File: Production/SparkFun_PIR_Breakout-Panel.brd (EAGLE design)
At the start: 204.5 x 152.1 mm, 1853 parts, among them U1 EKMC4607112k, U10 EKMC4607112k, U11 EKMC4607112k, U12 EKMC4607112k, U13 EKMC4607112k, U14 EKMC4607112k, U15 EKMC4607112k, U16 EKMC4607112k, U17 EKMC4607112k, U18 EKMC4607112k, U19 EKMC4607112k, U2 EKMC4607112k, U20 EKMC4607112k, U21 EKMC4607112k, U22 EKMC4607112k, U23 EKMC4607112k, U24 EKMC4607112k, U25 EKMC4607112k, U26 EKMC4607112k, U27 EKMC4607112k, U28 EKMC4607112k, U29 EKMC4607112k, U3 EKMC4607112k, U30 EKMC4607112k, U31 EKMC4607112k, U32 EKMC4607112k, U33 EKMC4607112k, U34 EKMC4607112k, U35 EKMC4607112k, U36 EKMC4607112k, U37 EKMC4607112k, U38 EKMC4607112k, U39 EKMC4607112k, U4 EKMC4607112k, U40 EKMC4607112k, U41 EKMC4607112k, U42 EKMC4607112k, U43 EKMC4607112k, U44 EKMC4607112k, U45 EKMC4607112k, U46 EKMC4607112k, U47 EKMC4607112k, U48 EKMC4607112k, U49 EKMC4607112k, U5 EKMC4607112k, U50 EKMC4607112k, U51 EKMC4607112k, U52 EKMC4607112k, U53 EKMC4607112k, U54 EKMC4607112k, U55 EKMC4607112k, U56 EKMC4607112k, U57 EKMC4607112k, U58 EKMC4607112k, U59 EKMC4607112k, U6 EKMC4607112k, U60 EKMC4607112k, U61 EKMC4607112k, U62 EKMC4607112k, U63 EKMC4607112k, U64 EKMC4607112k, U65 EKMC4607112k, U66 EKMC4607112k, U67 EKMC4607112k, U68 EKMC4607112k, U69 EKMC4607112k, U7 EKMC4607112k, U70 EKMC4607112k, U71 EKMC4607112k, U72 EKMC4607112k, U73 EKMC4607112k, U74 EKMC4607112k, U75 EKMC4607112k, U76 EKMC4607112k, U77 EKMC4607112k, U78 EKMC4607112k, U79 EKMC4607112k, U8 EKMC4607112k, U80 EKMC4607112k, U81 EKMC4607112k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

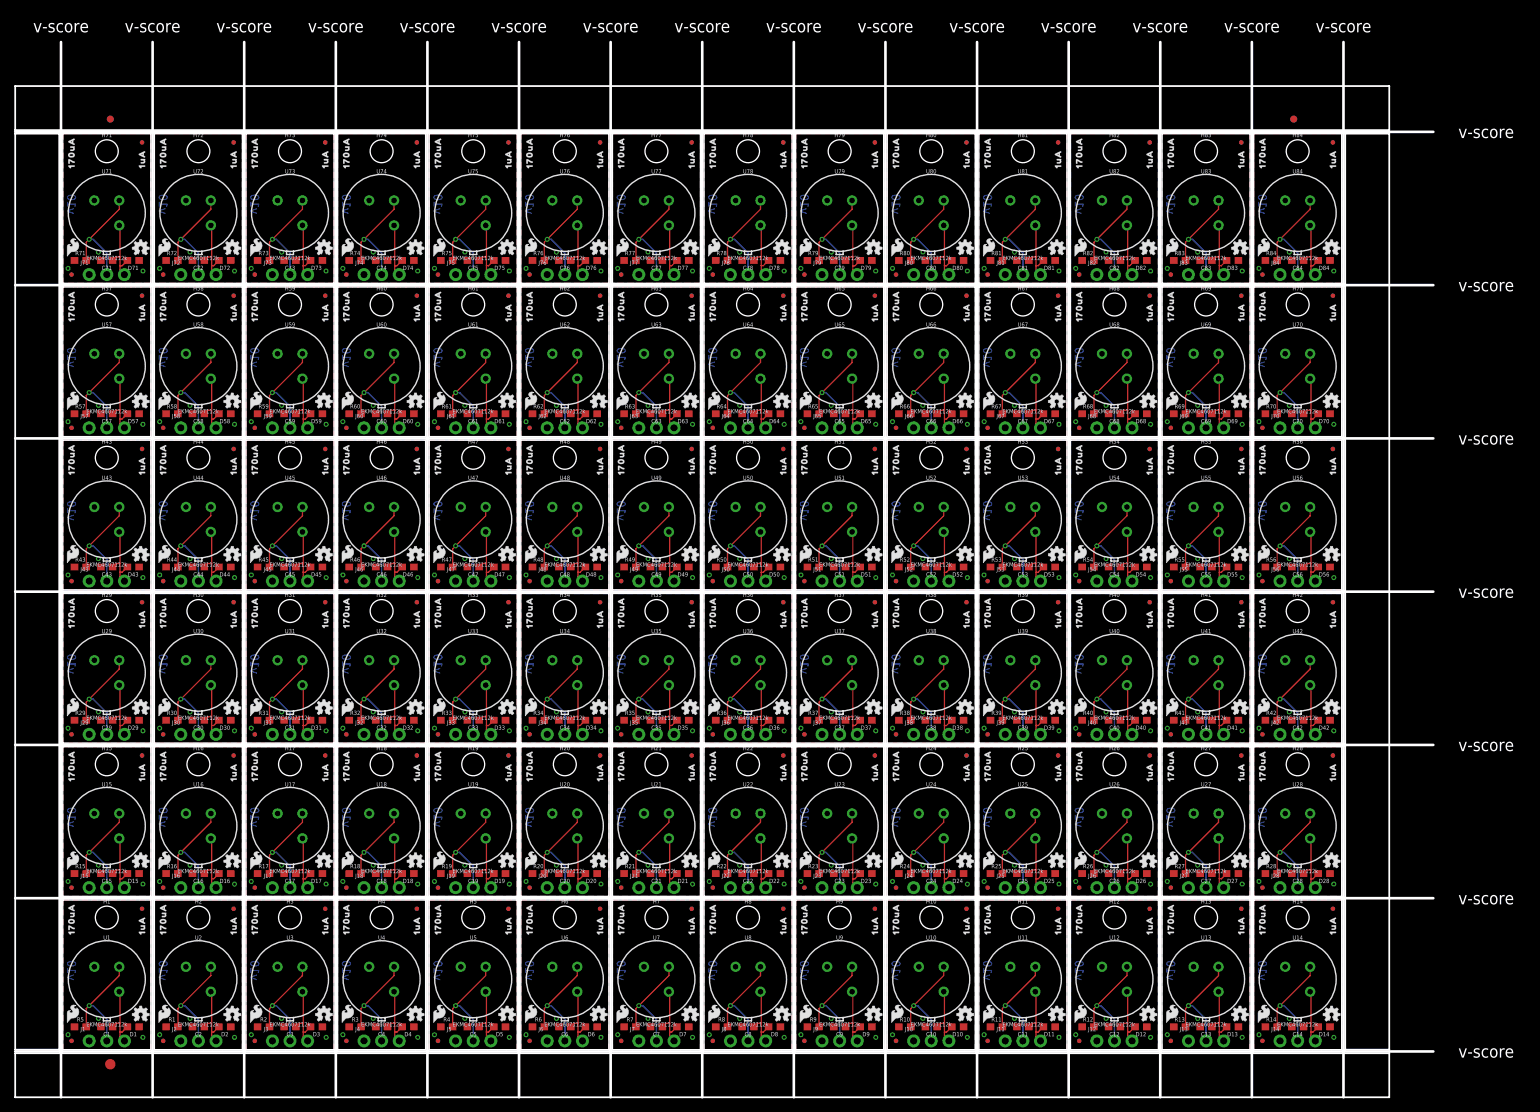
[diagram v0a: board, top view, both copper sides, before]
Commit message: adding fiducial to panel
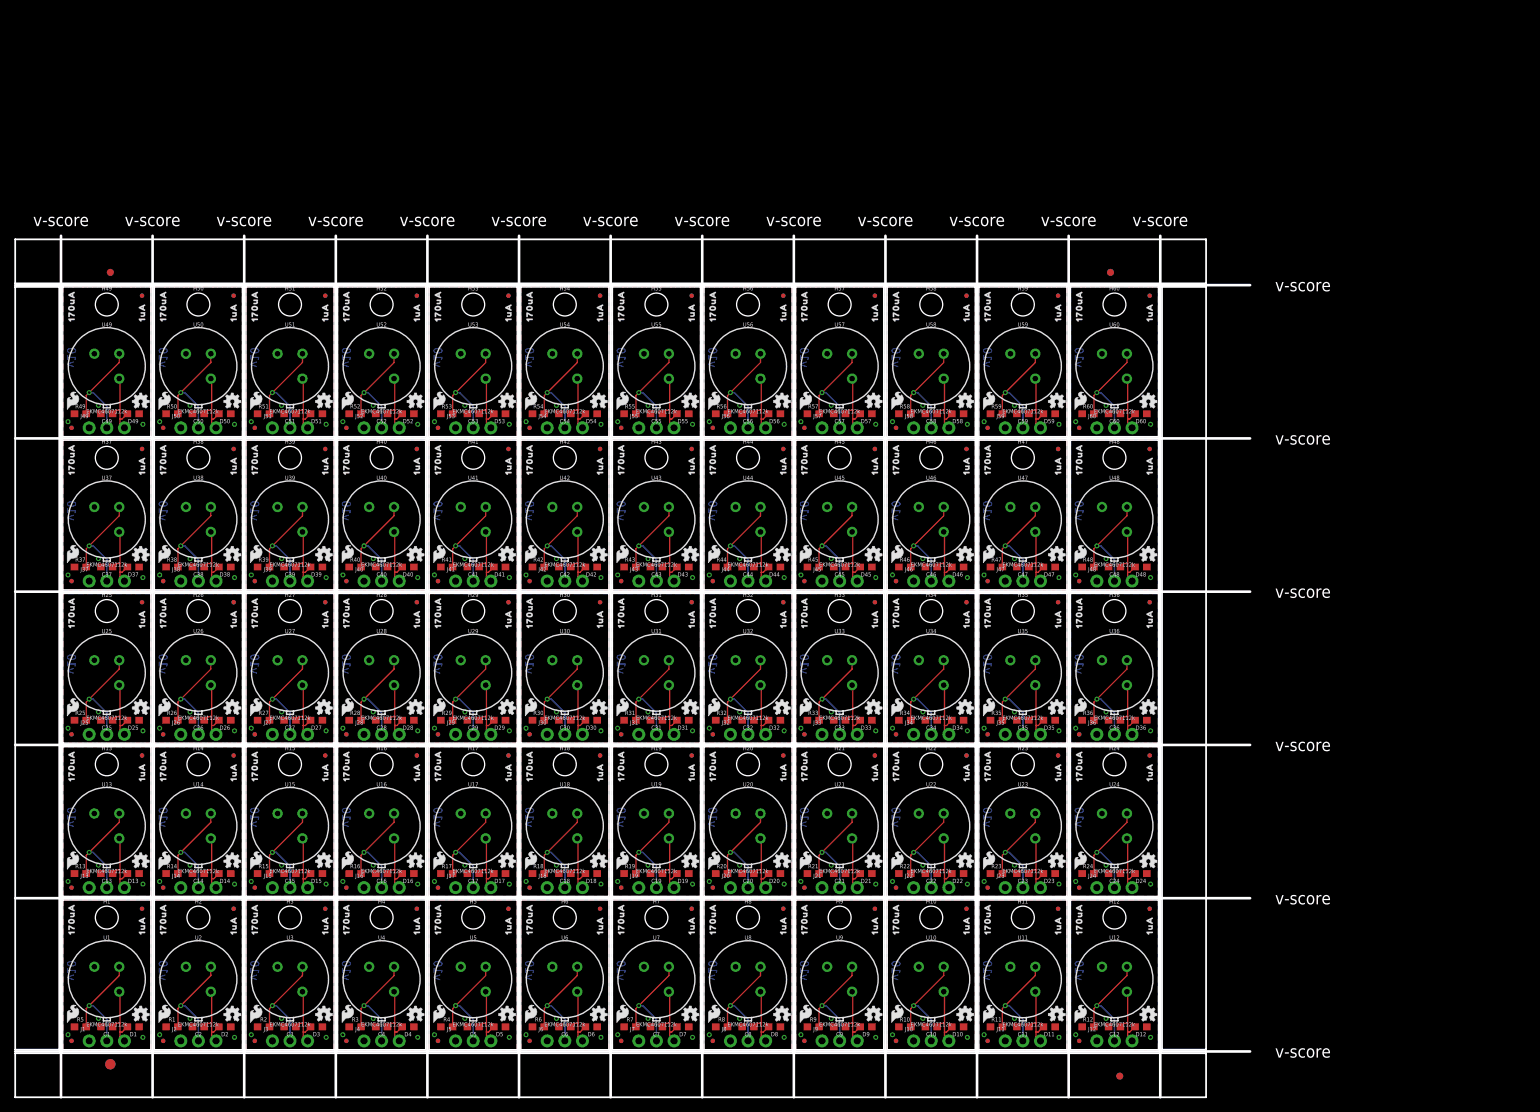
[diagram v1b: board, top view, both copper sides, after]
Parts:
- removed C61, C62, C63, C64, C65, C66, C67, C68, C69, C70, C71, C72, C73, C74, C75, C76, C77, C78, C79, C80, C81, C82, C83, C84: 0.1uF, SparkFun-Capacitors:0603
- removed D61, D62, D63, D64, D65, D66, D67, D68, D69, D70, D71, D72, D73, D74, D75, D76, D77, D78, D79, D80, D81, D82, D83, D84: 24V, SparkFun-DiscreteSemi:0603
- removed H61, H62, H63, H64, H65, H66, H67, H68, H69, H70, H71, H72, H73, H74, H75, H76, H77, H78, H79, H80, H81, H82, H83, H84: STAND-OFF, SparkFun-Hardware:STAND-OFF
- removed J61, J62, J63, J64, J65, J66, J67, J68, J69, J70, J71, J72, J73, J74, J75, J76, J77, J78, J79, J80, J81, J82, J83, J84: (no value), SparkFun-Connectors:1X03_NO_SILK
- removed JP241, JP242, JP243, JP244, JP245, JP246, JP247, JP248, JP249, JP250, JP251, JP252, JP253, JP254, JP255, JP256, JP257, JP258, JP259, JP260, JP261, JP262, JP263, JP264, JP265, JP266, JP267, JP268, JP269, JP270, JP271, JP272, JP273, JP274, JP275, JP276, JP277, JP278, JP279, JP280, JP281, JP282, JP283, JP284, JP285, JP286, JP287, JP288, JP289, JP290, JP291, JP292, JP293, JP294, JP295, JP296, JP297, JP298, JP299, JP300, JP301, JP302, JP303, JP304, JP305, JP306, JP307, JP308, JP309, JP310, JP311, JP312, JP313, JP314, JP315, JP316, JP317, JP318, JP319, JP320, JP321, JP322, JP323, JP324, JP325, JP326, JP327, JP328, JP329, JP330, JP331, JP332, JP333, JP334, JP335, JP336: FIDUCIALUFIDUCIAL, SparkFun:MICRO-FIDUCIAL
- removed LOGO181, LOGO184, LOGO187, LOGO190, LOGO193, LOGO196, LOGO199, LOGO202, LOGO205, LOGO208, LOGO211, LOGO214, LOGO217, LOGO220, LOGO223, LOGO226, LOGO229, LOGO232, LOGO235, LOGO238, LOGO241, LOGO244, LOGO247, LOGO250: OSHW-LOGOMINI, SparkFun-Aesthetics:OSHW-LOGO-MINI
- removed LOGO182, LOGO185, LOGO188, LOGO191, LOGO194, LOGO197, LOGO200, LOGO203, LOGO206, LOGO209, LOGO212, LOGO215, LOGO218, LOGO221, LOGO224, LOGO227, LOGO230, LOGO233, LOGO236, LOGO239, LOGO242, LOGO245, LOGO248, LOGO251: SFE_LOGO_NAME_FLAME.1_INCH, SparkFun-Aesthetics:SFE_LOGO_NAME_FLAME_.1
- removed LOGO183, LOGO186, LOGO189, LOGO192, LOGO195, LOGO198, LOGO201, LOGO204, LOGO207, LOGO210, LOGO213, LOGO216, LOGO219, LOGO222, LOGO225, LOGO228, LOGO231, LOGO234, LOGO237, LOGO240, LOGO243, LOGO246, LOGO249, LOGO252: SFE_LOGO_FLAME.1_INCH, SparkFun-Aesthetics:SFE_LOGO_FLAME_.1
- removed R61, R62, R63, R64, R65, R66, R67, R68, R69, R70, R71, R72, R73, R74, R75, R76, R77, R78, R79, R80, R81, R82, R83, R84: 47k, SparkFun-Resistors:0603
- removed U$541, U$550, U$559, U$568, U$577, U$586, U$595, U$604, U$613, U$622, U$631, U$640, U$649, U$658, U$667, U$676, U$685, U$694, U$703, U$712, U$721, U$730, U$739, U$748: (no value), output:PIR0
- removed U$542, U$551, U$560, U$569, U$578, U$587, U$596, U$605, U$614, U$623, U$632, U$641, U$650, U$659, U$668, U$677, U$686, U$695, U$704, U$713, U$722, U$731, U$740, U$749: (no value), output:170UA0
- removed U$543, U$552, U$561, U$570, U$579, U$588, U$597, U$606, U$615, U$624, U$633, U$642, U$651, U$660, U$669, U$678, U$687, U$696, U$705, U$714, U$723, U$732, U$741, U$750: (no value), output:1UA0
- removed U$544, U$553, U$562, U$571, U$580, U$589, U$598, U$607, U$616, U$625, U$634, U$643, U$652, U$661, U$670, U$679, U$688, U$697, U$706, U$715, U$724, U$733, U$742, U$751: (no value), output:BREAKOUT0
- removed U$545, U$554, U$563, U$572, U$581, U$590, U$599, U$608, U$617, U$626, U$635, U$644, U$653, U$662, U$671, U$680, U$689, U$698, U$707, U$716, U$725, U$734, U$743, U$752: (no value), output:#OUT#0
- removed U$546, U$555, U$564, U$573, U$582, U$591, U$600, U$609, U$618, U$627, U$636, U$645, U$654, U$663, U$672, U$681, U$690, U$699, U$708, U$717, U$726, U$735, U$744, U$753: (no value), output:#3V3#0
- removed U$547, U$556, U$565, U$574, U$583, U$592, U$601, U$610, U$619, U$628, U$637, U$646, U$655, U$664, U$673, U$682, U$691, U$700, U$709, U$718, U$727, U$736, U$745, U$754: (no value), output:#GND#0
- removed U$548, U$557, U$566, U$575, U$584, U$593, U$602, U$611, U$620, U$629, U$638, U$647, U$656, U$665, U$674, U$683, U$692, U$701, U$710, U$719, U$728, U$737, U$746, U$755: (no value), output:X0
- removed U$549, U$558, U$567, U$576, U$585, U$594, U$603, U$612, U$621, U$630, U$639, U$648, U$657, U$666, U$675, U$684, U$693, U$702, U$711, U$720, U$729, U$738, U$747, U$756: (no value), output:Y0
- removed U61, U62, U63, U64, U65, U66, U67, U68, U69, U70, U71, U72, U73, U74, U75, U76, U77, U78, U79, U80, U81, U82, U83, U84: EKMC4607112k, SparkFun-Sensors:TO-3
- added E$6: (no value), SparkFun-Retired:FIDUCIAL-1.5X3
- added E$7, E$8: (no value), SparkFun-Aesthetics:FIDUCIAL-1X2
- moved C13 160.0 mm to (6.35, 25.4)
- moved C14 160.0 mm to (19.6, 25.4)
- moved D13 160.0 mm to (10.2, 25.4)
- moved D14 160.0 mm to (23.4, 25.4)
- moved H13 160.0 mm to (6.35, 41.1)
- moved H14 160.0 mm to (19.6, 41.1)
- moved J13 160.0 mm to (3.81, 23.4)
- moved J14 160.0 mm to (17.0, 23.4)
- moved LOGO37 160.0 mm to (11.2, 27.2)
- moved LOGO38 160.0 mm to (6.35, 36.1)
- moved LOGO39 160.0 mm to (1.46, 27.3)
- moved LOGO40 160.0 mm to (24.4, 27.2)
- moved LOGO41 160.0 mm to (19.6, 36.1)
- moved LOGO42 160.0 mm to (14.7, 27.3)
- moved R13 160.0 mm to (2.54, 25.4)
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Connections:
- removed net 3.3V60: C61.1, D61.2, J61.3, U61.VDD
- removed net 3.3V61: C62.1, D62.2, J62.3, U62.VDD
- removed net 3.3V62: C63.1, D63.2, J63.3, U63.VDD
- removed net 3.3V63: C64.1, D64.2, J64.3, U64.VDD
- removed net 3.3V64: C65.1, D65.2, J65.3, U65.VDD
- removed net 3.3V65: C66.1, D66.2, J66.3, U66.VDD
- removed net 3.3V66: C67.1, D67.2, J67.3, U67.VDD
- removed net 3.3V67: C68.1, D68.2, J68.3, U68.VDD
- removed net 3.3V68: C69.1, D69.2, J69.3, U69.VDD
- removed net 3.3V69: C70.1, D70.2, J70.3, U70.VDD
- removed net 3.3V70: C71.1, D71.2, J71.3, U71.VDD
- removed net 3.3V71: C72.1, D72.2, J72.3, U72.VDD
- removed net 3.3V72: C73.1, D73.2, J73.3, U73.VDD
- removed net 3.3V73: C74.1, D74.2, J74.3, U74.VDD
- removed net 3.3V74: C75.1, D75.2, J75.3, U75.VDD
- removed net 3.3V75: C76.1, D76.2, J76.3, U76.VDD
- removed net 3.3V76: C77.1, D77.2, J77.3, U77.VDD
- removed net 3.3V77: C78.1, D78.2, J78.3, U78.VDD
- removed net 3.3V78: C79.1, D79.2, J79.3, U79.VDD
- removed net 3.3V79: C80.1, D80.2, J80.3, U80.VDD
- removed net 3.3V80: C81.1, D81.2, J81.3, U81.VDD
- removed net 3.3V81: C82.1, D82.2, J82.3, U82.VDD
- removed net 3.3V82: C83.1, D83.2, J83.3, U83.VDD
- removed net 3.3V83: C84.1, D84.2, J84.3, U84.VDD
- removed net GND60: C61.2, D61.1, J61.1, R61.1, U61.GND
- removed net GND61: C62.2, D62.1, J62.1, R62.1, U62.GND
- removed net GND62: C63.2, D63.1, J63.1, R63.1, U63.GND
- removed net GND63: C64.2, D64.1, J64.1, R64.1, U64.GND
- removed net GND64: C65.2, D65.1, J65.1, R65.1, U65.GND
- removed net GND65: C66.2, D66.1, J66.1, R66.1, U66.GND
- removed net GND66: C67.2, D67.1, J67.1, R67.1, U67.GND
- removed net GND67: C68.2, D68.1, J68.1, R68.1, U68.GND
- removed net GND68: C69.2, D69.1, J69.1, R69.1, U69.GND
- removed net GND69: C70.2, D70.1, J70.1, R70.1, U70.GND
- removed net GND70: C71.2, D71.1, J71.1, R71.1, U71.GND
- removed net GND71: C72.2, D72.1, J72.1, R72.1, U72.GND
- removed net GND72: C73.2, D73.1, J73.1, R73.1, U73.GND
- removed net GND73: C74.2, D74.1, J74.1, R74.1, U74.GND
- removed net GND74: C75.2, D75.1, J75.1, R75.1, U75.GND
- removed net GND75: C76.2, D76.1, J76.1, R76.1, U76.GND
- removed net GND76: C77.2, D77.1, J77.1, R77.1, U77.GND
- removed net GND77: C78.2, D78.1, J78.1, R78.1, U78.GND
- removed net GND78: C79.2, D79.1, J79.1, R79.1, U79.GND
- removed net GND79: C80.2, D80.1, J80.1, R80.1, U80.GND
- removed net GND80: C81.2, D81.1, J81.1, R81.1, U81.GND
- removed net GND81: C82.2, D82.1, J82.1, R82.1, U82.GND
- removed net GND82: C83.2, D83.1, J83.1, R83.1, U83.GND
- removed net GND83: C84.2, D84.1, J84.1, R84.1, U84.GND
- removed net PIR_OUT60: J61.2, R61.2, U61.OUT
- removed net PIR_OUT61: J62.2, R62.2, U62.OUT
- removed net PIR_OUT62: J63.2, R63.2, U63.OUT
- removed net PIR_OUT63: J64.2, R64.2, U64.OUT
- removed net PIR_OUT64: J65.2, R65.2, U65.OUT
- removed net PIR_OUT65: J66.2, R66.2, U66.OUT
- removed net PIR_OUT66: J67.2, R67.2, U67.OUT
- removed net PIR_OUT67: J68.2, R68.2, U68.OUT
- removed net PIR_OUT68: J69.2, R69.2, U69.OUT
- removed net PIR_OUT69: J70.2, R70.2, U70.OUT
- removed net PIR_OUT70: J71.2, R71.2, U71.OUT
- removed net PIR_OUT71: J72.2, R72.2, U72.OUT
- removed net PIR_OUT72: J73.2, R73.2, U73.OUT
- removed net PIR_OUT73: J74.2, R74.2, U74.OUT
- removed net PIR_OUT74: J75.2, R75.2, U75.OUT
- removed net PIR_OUT75: J76.2, R76.2, U76.OUT
- removed net PIR_OUT76: J77.2, R77.2, U77.OUT
- removed net PIR_OUT77: J78.2, R78.2, U78.OUT
- removed net PIR_OUT78: J79.2, R79.2, U79.OUT
- removed net PIR_OUT79: J80.2, R80.2, U80.OUT
- removed net PIR_OUT80: J81.2, R81.2, U81.OUT
- removed net PIR_OUT81: J82.2, R82.2, U82.OUT
- removed net PIR_OUT82: J83.2, R83.2, U83.OUT
- removed net PIR_OUT83: J84.2, R84.2, U84.OUT
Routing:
- net PIR_OUT80: track 17.1 -> 0.00 mm, vias 1 -> 0
- net PIR_OUT66: track 17.1 -> 0.00 mm, vias 1 -> 0
- net PIR_OUT75: track 17.1 -> 0.00 mm, vias 1 -> 0
- net PIR_OUT61: track 17.1 -> 0.00 mm, vias 1 -> 0
- net PIR_OUT70: track 17.1 -> 0.00 mm, vias 1 -> 0
- net PIR_OUT74: track 17.1 -> 0.00 mm, vias 1 -> 0
- net PIR_OUT73: track 17.1 -> 0.00 mm, vias 1 -> 0
- net PIR_OUT72: track 17.1 -> 0.00 mm, vias 1 -> 0
- net PIR_OUT71: track 17.1 -> 0.00 mm, vias 1 -> 0
- net PIR_OUT60: track 17.1 -> 0.00 mm, vias 1 -> 0
- net PIR_OUT79: track 17.1 -> 0.00 mm, vias 1 -> 0
- net PIR_OUT78: track 17.1 -> 0.00 mm, vias 1 -> 0
- net PIR_OUT77: track 17.1 -> 0.00 mm, vias 1 -> 0
- net PIR_OUT65: track 17.1 -> 0.00 mm, vias 1 -> 0
- net PIR_OUT64: track 17.1 -> 0.00 mm, vias 1 -> 0
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- removed copper zone on layer 1, net GND60
- removed copper zone on layer 16, net GND60
- removed copper zone on layer 1, net GND61
- removed copper zone on layer 16, net GND61
- removed copper zone on layer 1, net GND62
- removed copper zone on layer 16, net GND62
- removed copper zone on layer 1, net GND63
- removed copper zone on layer 16, net GND63
- removed copper zone on layer 1, net GND64
- removed copper zone on layer 16, net GND64
- removed copper zone on layer 1, net GND65
- removed copper zone on layer 16, net GND65
- removed copper zone on layer 1, net GND66
- removed copper zone on layer 16, net GND66
- removed copper zone on layer 1, net GND67
- removed copper zone on layer 16, net GND67
- removed copper zone on layer 1, net GND68
- removed copper zone on layer 16, net GND68
- removed copper zone on layer 1, net GND69
- removed copper zone on layer 16, net GND69
- removed copper zone on layer 1, net GND70
- removed copper zone on layer 16, net GND70
- removed copper zone on layer 1, net GND71
- removed copper zone on layer 16, net GND71
- removed copper zone on layer 1, net GND72
- removed copper zone on layer 16, net GND72
- removed copper zone on layer 1, net GND73
- removed copper zone on layer 16, net GND73
- removed copper zone on layer 1, net GND74
- removed copper zone on layer 16, net GND74
- removed copper zone on layer 1, net GND75
- removed copper zone on layer 16, net GND75
- removed copper zone on layer 1, net GND76
- removed copper zone on layer 16, net GND76
- removed copper zone on layer 1, net GND77
- removed copper zone on layer 16, net GND77
- removed copper zone on layer 1, net GND78
- removed copper zone on layer 16, net GND78
- removed copper zone on layer 1, net GND79
- removed copper zone on layer 16, net GND79
- removed copper zone on layer 1, net GND80
- removed copper zone on layer 16, net GND80
- removed copper zone on layer 1, net GND81
- removed copper zone on layer 16, net GND81
- removed copper zone on layer 1, net GND82
- removed copper zone on layer 16, net GND82
- removed copper zone on layer 1, net GND83
- removed copper zone on layer 16, net GND83
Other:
- board size 204.5 x 152.1 mm -> 178.1 x 124.2 mm

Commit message: removing fiducial
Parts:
- removed E$7, E$8: (no value), SparkFun-Aesthetics:FIDUCIAL-1X2
- added C61, C62, C63, C64, C65, C66, C67, C68, C69, C70, C71, C72, C73, C74, C75, C76, C77, C78, C79, C80, C81, C82, C83, C84: 0.1uF, SparkFun-Capacitors:0603
- added D61, D62, D63, D64, D65, D66, D67, D68, D69, D70, D71, D72, D73, D74, D75, D76, D77, D78, D79, D80, D81, D82, D83, D84: 24V, SparkFun-DiscreteSemi:0603
- added H61, H62, H63, H64, H65, H66, H67, H68, H69, H70, H71, H72, H73, H74, H75, H76, H77, H78, H79, H80, H81, H82, H83, H84: STAND-OFF, SparkFun-Hardware:STAND-OFF
- added J61, J62, J63, J64, J65, J66, J67, J68, J69, J70, J71, J72, J73, J74, J75, J76, J77, J78, J79, J80, J81, J82, J83, J84: (no value), SparkFun-Connectors:1X03_NO_SILK
- added JP241, JP242, JP243, JP244, JP245, JP246, JP247, JP248, JP249, JP250, JP251, JP252, JP253, JP254, JP255, JP256, JP257, JP258, JP259, JP260, JP261, JP262, JP263, JP264, JP265, JP266, JP267, JP268, JP269, JP270, JP271, JP272, JP273, JP274, JP275, JP276, JP277, JP278, JP279, JP280, JP281, JP282, JP283, JP284, JP285, JP286, JP287, JP288, JP289, JP290, JP291, JP292, JP293, JP294, JP295, JP296, JP297, JP298, JP299, JP300, JP301, JP302, JP303, JP304, JP305, JP306, JP307, JP308, JP309, JP310, JP311, JP312, JP313, JP314, JP315, JP316, JP317, JP318, JP319, JP320, JP321, JP322, JP323, JP324, JP325, JP326, JP327, JP328, JP329, JP330, JP331, JP332, JP333, JP334, JP335, JP336: FIDUCIALUFIDUCIAL, SparkFun:MICRO-FIDUCIAL
- added LOGO181, LOGO184, LOGO187, LOGO190, LOGO193, LOGO196, LOGO199, LOGO202, LOGO205, LOGO208, LOGO211, LOGO214, LOGO217, LOGO220, LOGO223, LOGO226, LOGO229, LOGO232, LOGO235, LOGO238, LOGO241, LOGO244, LOGO247, LOGO250: OSHW-LOGOMINI, SparkFun-Aesthetics:OSHW-LOGO-MINI
- added LOGO182, LOGO185, LOGO188, LOGO191, LOGO194, LOGO197, LOGO200, LOGO203, LOGO206, LOGO209, LOGO212, LOGO215, LOGO218, LOGO221, LOGO224, LOGO227, LOGO230, LOGO233, LOGO236, LOGO239, LOGO242, LOGO245, LOGO248, LOGO251: SFE_LOGO_NAME_FLAME.1_INCH, SparkFun-Aesthetics:SFE_LOGO_NAME_FLAME_.1
- added LOGO183, LOGO186, LOGO189, LOGO192, LOGO195, LOGO198, LOGO201, LOGO204, LOGO207, LOGO210, LOGO213, LOGO216, LOGO219, LOGO222, LOGO225, LOGO228, LOGO231, LOGO234, LOGO237, LOGO240, LOGO243, LOGO246, LOGO249, LOGO252: SFE_LOGO_FLAME.1_INCH, SparkFun-Aesthetics:SFE_LOGO_FLAME_.1
- added R61, R62, R63, R64, R65, R66, R67, R68, R69, R70, R71, R72, R73, R74, R75, R76, R77, R78, R79, R80, R81, R82, R83, R84: 47k, SparkFun-Resistors:0603
- added U$541, U$550, U$559, U$568, U$577, U$586, U$595, U$604, U$613, U$622, U$631, U$640, U$649, U$658, U$667, U$676, U$685, U$694, U$703, U$712, U$721, U$730, U$739, U$748: (no value), output:PIR0
- added U$542, U$551, U$560, U$569, U$578, U$587, U$596, U$605, U$614, U$623, U$632, U$641, U$650, U$659, U$668, U$677, U$686, U$695, U$704, U$713, U$722, U$731, U$740, U$749: (no value), output:170UA0
- added U$543, U$552, U$561, U$570, U$579, U$588, U$597, U$606, U$615, U$624, U$633, U$642, U$651, U$660, U$669, U$678, U$687, U$696, U$705, U$714, U$723, U$732, U$741, U$750: (no value), output:1UA0
- added U$544, U$553, U$562, U$571, U$580, U$589, U$598, U$607, U$616, U$625, U$634, U$643, U$652, U$661, U$670, U$679, U$688, U$697, U$706, U$715, U$724, U$733, U$742, U$751: (no value), output:BREAKOUT0
- added U$545, U$554, U$563, U$572, U$581, U$590, U$599, U$608, U$617, U$626, U$635, U$644, U$653, U$662, U$671, U$680, U$689, U$698, U$707, U$716, U$725, U$734, U$743, U$752: (no value), output:#OUT#0
- added U$546, U$555, U$564, U$573, U$582, U$591, U$600, U$609, U$618, U$627, U$636, U$645, U$654, U$663, U$672, U$681, U$690, U$699, U$708, U$717, U$726, U$735, U$744, U$753: (no value), output:#3V3#0
- added U$547, U$556, U$565, U$574, U$583, U$592, U$601, U$610, U$619, U$628, U$637, U$646, U$655, U$664, U$673, U$682, U$691, U$700, U$709, U$718, U$727, U$736, U$745, U$754: (no value), output:#GND#0
- added U$548, U$557, U$566, U$575, U$584, U$593, U$602, U$611, U$620, U$629, U$638, U$647, U$656, U$665, U$674, U$683, U$692, U$701, U$710, U$719, U$728, U$737, U$746, U$755: (no value), output:X0
- added U$549, U$558, U$567, U$576, U$585, U$594, U$603, U$612, U$621, U$630, U$639, U$648, U$657, U$666, U$675, U$684, U$693, U$702, U$711, U$720, U$729, U$738, U$747, U$756: (no value), output:Y0
- added U61, U62, U63, U64, U65, U66, U67, U68, U69, U70, U71, U72, U73, U74, U75, U76, U77, U78, U79, U80, U81, U82, U83, U84: EKMC4607112k, SparkFun-Sensors:TO-3
- moved C13 160.0 mm to (164.8, 3.30)
- moved C14 160.0 mm to (178.1, 3.30)
- moved D13 160.0 mm to (168.7, 3.30)
- moved D14 160.0 mm to (181.9, 3.30)
- moved H13 160.0 mm to (164.8, 19.1)
- moved H14 160.0 mm to (178.1, 19.1)
- moved J13 160.0 mm to (162.3, 1.27)
- moved J14 160.0 mm to (175.5, 1.27)
- moved LOGO37 160.0 mm to (169.7, 5.08)
- moved LOGO38 160.0 mm to (164.8, 14.0)
- moved LOGO39 160.0 mm to (160.0, 5.21)
- moved LOGO40 160.0 mm to (182.9, 5.08)
- moved LOGO41 160.0 mm to (178.1, 14.0)
- moved LOGO42 160.0 mm to (173.2, 5.21)
- moved R13 160.0 mm to (161.0, 3.30)
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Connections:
- new net 3.3V60: C61.1, D61.2, J61.3, U61.VDD
- new net 3.3V61: C62.1, D62.2, J62.3, U62.VDD
- new net 3.3V62: C63.1, D63.2, J63.3, U63.VDD
- new net 3.3V63: C64.1, D64.2, J64.3, U64.VDD
- new net 3.3V64: C65.1, D65.2, J65.3, U65.VDD
- new net 3.3V65: C66.1, D66.2, J66.3, U66.VDD
- new net 3.3V66: C67.1, D67.2, J67.3, U67.VDD
- new net 3.3V67: C68.1, D68.2, J68.3, U68.VDD
- new net 3.3V68: C69.1, D69.2, J69.3, U69.VDD
- new net 3.3V69: C70.1, D70.2, J70.3, U70.VDD
- new net 3.3V70: C71.1, D71.2, J71.3, U71.VDD
- new net 3.3V71: C72.1, D72.2, J72.3, U72.VDD
- new net 3.3V72: C73.1, D73.2, J73.3, U73.VDD
- new net 3.3V73: C74.1, D74.2, J74.3, U74.VDD
- new net 3.3V74: C75.1, D75.2, J75.3, U75.VDD
- new net 3.3V75: C76.1, D76.2, J76.3, U76.VDD
- new net 3.3V76: C77.1, D77.2, J77.3, U77.VDD
- new net 3.3V77: C78.1, D78.2, J78.3, U78.VDD
- new net 3.3V78: C79.1, D79.2, J79.3, U79.VDD
- new net 3.3V79: C80.1, D80.2, J80.3, U80.VDD
- new net 3.3V80: C81.1, D81.2, J81.3, U81.VDD
- new net 3.3V81: C82.1, D82.2, J82.3, U82.VDD
- new net 3.3V82: C83.1, D83.2, J83.3, U83.VDD
- new net 3.3V83: C84.1, D84.2, J84.3, U84.VDD
- new net GND60: C61.2, D61.1, J61.1, R61.1, U61.GND
- new net GND61: C62.2, D62.1, J62.1, R62.1, U62.GND
- new net GND62: C63.2, D63.1, J63.1, R63.1, U63.GND
- new net GND63: C64.2, D64.1, J64.1, R64.1, U64.GND
- new net GND64: C65.2, D65.1, J65.1, R65.1, U65.GND
- new net GND65: C66.2, D66.1, J66.1, R66.1, U66.GND
- new net GND66: C67.2, D67.1, J67.1, R67.1, U67.GND
- new net GND67: C68.2, D68.1, J68.1, R68.1, U68.GND
- new net GND68: C69.2, D69.1, J69.1, R69.1, U69.GND
- new net GND69: C70.2, D70.1, J70.1, R70.1, U70.GND
- new net GND70: C71.2, D71.1, J71.1, R71.1, U71.GND
- new net GND71: C72.2, D72.1, J72.1, R72.1, U72.GND
- new net GND72: C73.2, D73.1, J73.1, R73.1, U73.GND
- new net GND73: C74.2, D74.1, J74.1, R74.1, U74.GND
- new net GND74: C75.2, D75.1, J75.1, R75.1, U75.GND
- new net GND75: C76.2, D76.1, J76.1, R76.1, U76.GND
- new net GND76: C77.2, D77.1, J77.1, R77.1, U77.GND
- new net GND77: C78.2, D78.1, J78.1, R78.1, U78.GND
- new net GND78: C79.2, D79.1, J79.1, R79.1, U79.GND
- new net GND79: C80.2, D80.1, J80.1, R80.1, U80.GND
- new net GND80: C81.2, D81.1, J81.1, R81.1, U81.GND
- new net GND81: C82.2, D82.1, J82.1, R82.1, U82.GND
- new net GND82: C83.2, D83.1, J83.1, R83.1, U83.GND
- new net GND83: C84.2, D84.1, J84.1, R84.1, U84.GND
- new net PIR_OUT60: J61.2, R61.2, U61.OUT
- new net PIR_OUT61: J62.2, R62.2, U62.OUT
- new net PIR_OUT62: J63.2, R63.2, U63.OUT
- new net PIR_OUT63: J64.2, R64.2, U64.OUT
- new net PIR_OUT64: J65.2, R65.2, U65.OUT
- new net PIR_OUT65: J66.2, R66.2, U66.OUT
- new net PIR_OUT66: J67.2, R67.2, U67.OUT
- new net PIR_OUT67: J68.2, R68.2, U68.OUT
- new net PIR_OUT68: J69.2, R69.2, U69.OUT
- new net PIR_OUT69: J70.2, R70.2, U70.OUT
- new net PIR_OUT70: J71.2, R71.2, U71.OUT
- new net PIR_OUT71: J72.2, R72.2, U72.OUT
- new net PIR_OUT72: J73.2, R73.2, U73.OUT
- new net PIR_OUT73: J74.2, R74.2, U74.OUT
- new net PIR_OUT74: J75.2, R75.2, U75.OUT
- new net PIR_OUT75: J76.2, R76.2, U76.OUT
- new net PIR_OUT76: J77.2, R77.2, U77.OUT
- new net PIR_OUT77: J78.2, R78.2, U78.OUT
- new net PIR_OUT78: J79.2, R79.2, U79.OUT
- new net PIR_OUT79: J80.2, R80.2, U80.OUT
- new net PIR_OUT80: J81.2, R81.2, U81.OUT
- new net PIR_OUT81: J82.2, R82.2, U82.OUT
- new net PIR_OUT82: J83.2, R83.2, U83.OUT
- new net PIR_OUT83: J84.2, R84.2, U84.OUT
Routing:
- net PIR_OUT80: track 0.00 -> 17.1 mm, vias 0 -> 1
- net PIR_OUT66: track 0.00 -> 17.1 mm, vias 0 -> 1
- net PIR_OUT75: track 0.00 -> 17.1 mm, vias 0 -> 1
- net PIR_OUT61: track 0.00 -> 17.1 mm, vias 0 -> 1
- net PIR_OUT70: track 0.00 -> 17.1 mm, vias 0 -> 1
- net PIR_OUT74: track 0.00 -> 17.1 mm, vias 0 -> 1
- net PIR_OUT73: track 0.00 -> 17.1 mm, vias 0 -> 1
- net PIR_OUT72: track 0.00 -> 17.1 mm, vias 0 -> 1
- net PIR_OUT71: track 0.00 -> 17.1 mm, vias 0 -> 1
- net PIR_OUT60: track 0.00 -> 17.1 mm, vias 0 -> 1
- net PIR_OUT79: track 0.00 -> 17.1 mm, vias 0 -> 1
- net PIR_OUT78: track 0.00 -> 17.1 mm, vias 0 -> 1
- net PIR_OUT77: track 0.00 -> 17.1 mm, vias 0 -> 1
- net PIR_OUT65: track 0.00 -> 17.1 mm, vias 0 -> 1
- net PIR_OUT64: track 0.00 -> 17.1 mm, vias 0 -> 1
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- added copper zone on layer 1, net GND60
- added copper zone on layer 16, net GND60
- added copper zone on layer 1, net GND61
- added copper zone on layer 16, net GND61
- added copper zone on layer 1, net GND62
- added copper zone on layer 16, net GND62
- added copper zone on layer 1, net GND63
- added copper zone on layer 16, net GND63
- added copper zone on layer 1, net GND64
- added copper zone on layer 16, net GND64
- added copper zone on layer 1, net GND65
- added copper zone on layer 16, net GND65
- added copper zone on layer 1, net GND66
- added copper zone on layer 16, net GND66
- added copper zone on layer 1, net GND67
- added copper zone on layer 16, net GND67
- added copper zone on layer 1, net GND68
- added copper zone on layer 16, net GND68
- added copper zone on layer 1, net GND69
- added copper zone on layer 16, net GND69
- added copper zone on layer 1, net GND70
- added copper zone on layer 16, net GND70
- added copper zone on layer 1, net GND71
- added copper zone on layer 16, net GND71
- added copper zone on layer 1, net GND72
- added copper zone on layer 16, net GND72
- added copper zone on layer 1, net GND73
- added copper zone on layer 16, net GND73
- added copper zone on layer 1, net GND74
- added copper zone on layer 16, net GND74
- added copper zone on layer 1, net GND75
- added copper zone on layer 16, net GND75
- added copper zone on layer 1, net GND76
- added copper zone on layer 16, net GND76
- added copper zone on layer 1, net GND77
- added copper zone on layer 16, net GND77
- added copper zone on layer 1, net GND78
- added copper zone on layer 16, net GND78
- added copper zone on layer 1, net GND79
- added copper zone on layer 16, net GND79
- added copper zone on layer 1, net GND80
- added copper zone on layer 16, net GND80
- added copper zone on layer 1, net GND81
- added copper zone on layer 16, net GND81
- added copper zone on layer 1, net GND82
- added copper zone on layer 16, net GND82
- added copper zone on layer 1, net GND83
- added copper zone on layer 16, net GND83
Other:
- board size 178.1 x 124.2 mm -> 204.5 x 146.3 mm
